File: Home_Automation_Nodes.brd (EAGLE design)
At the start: 121 x 70 mm, 19 parts

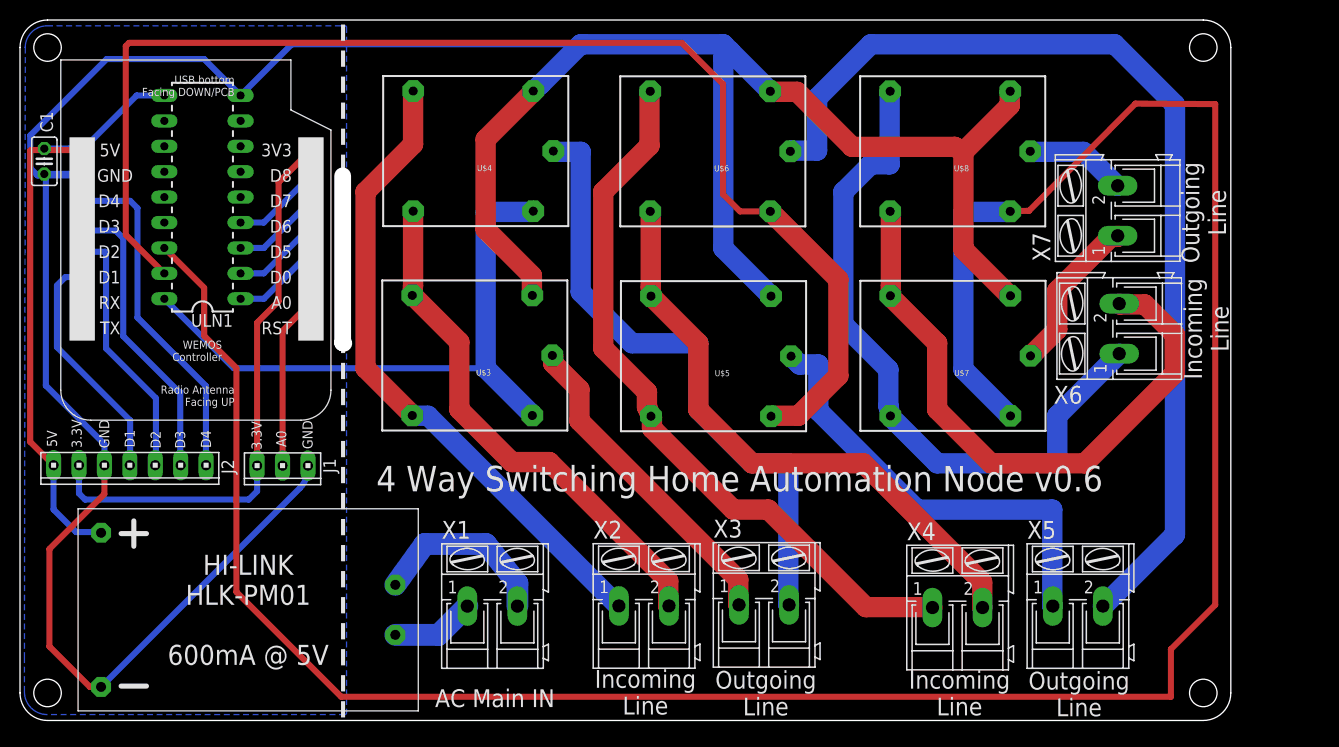
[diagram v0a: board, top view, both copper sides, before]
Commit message: ULN connection fix. Changed coil connection from GND to 5V
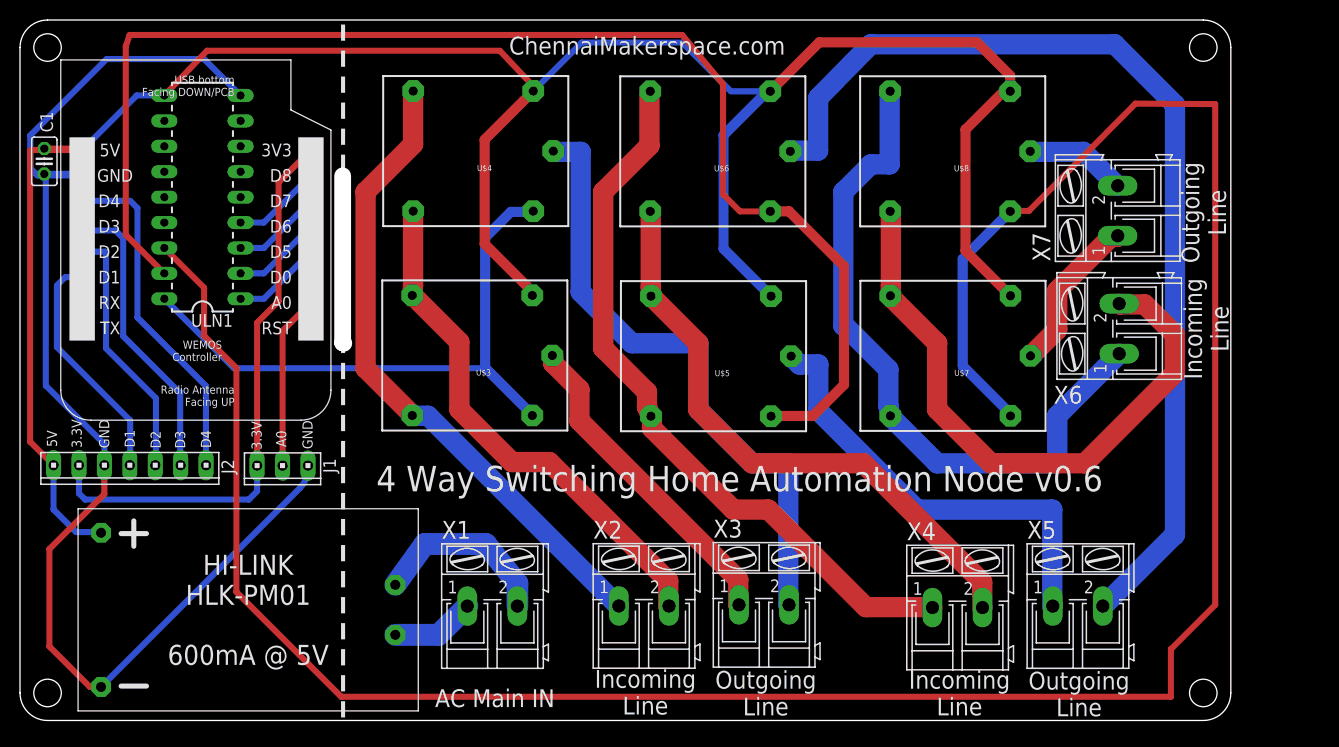
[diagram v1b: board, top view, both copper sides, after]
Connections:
- net 5V: now also U$3.COIL0, U$4.COIL0, U$5.COIL0, U$6.COIL0, U$7.COIL0, U$8.COIL0
- net GND: no longer U$3.COIL0, U$4.COIL0, U$5.COIL0, U$6.COIL0, U$7.COIL0, U$8.COIL0
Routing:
- net 5V: track 62.1 -> 233.0 mm, vias 0 -> 1
- net GND: track 288.8 -> 127.7 mm
- net RELAY2: track 129.9 -> 133.6 mm
- net RELAY3: track 248.2 -> 245.6 mm
- net RELAY1: track 62.1 -> 60.6 mm
- removed copper zone on layer 16, net GND
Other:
- board text added: "ChennaiMakerspace.com"

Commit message: Changes: 1. WeMos D1 Mini Pads modified 2. Pins to ULN changed, to free the SPI channels 3. GND Plane added
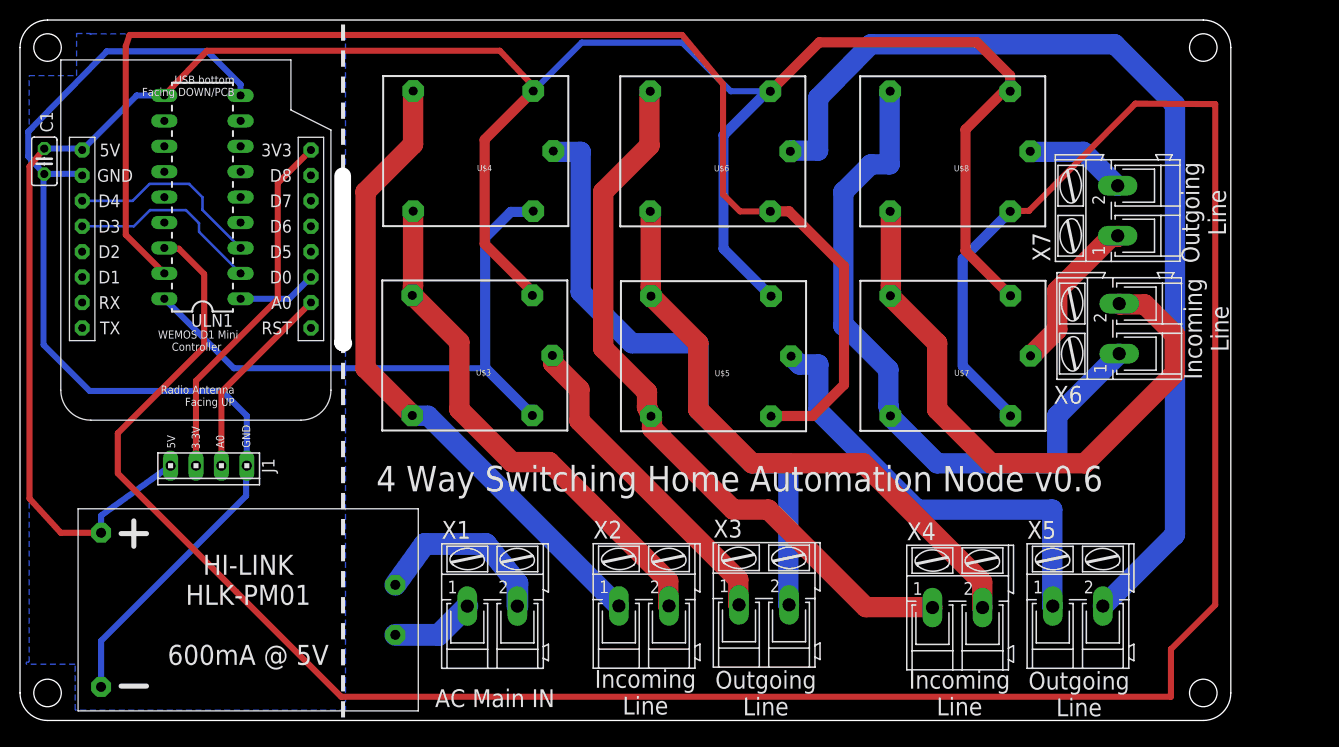
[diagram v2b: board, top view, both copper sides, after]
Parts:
- removed J2: (no value), con-amp:10X07MTA
- J1: device con-amp:10X03MTA -> con-amp:10X04MTA
- ULN1: value (none) -> ULN2803
- moved J1 7.38 mm to (18.9, 25.5)
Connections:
- removed net D3: J2.6, U$1.D3
- removed net D4: J2.7, U$1.D4
- removed net RELAY4: ULN1.15
- removed net SW4: U$1.D8, ULN1.4
- new net D5: U$1.D5
- new net D6: U$1.D6
- new net D7: U$1.D7
- net 3.3V: now also J1.2; no longer J1.1, J2.2
- net 5V: now also J1.1; no longer J2.1
- net A0: now also J1.3; no longer J1.2
- net D1: no longer J2.4
- net D2: no longer J2.5
- net GND: now also J1.4; no longer J1.3, J2.3
- net SW1: now also U$1.D0; no longer U$1.D5
- net SW2: now also U$1.D3; no longer U$1.D6
- net SW3: now also U$1.D4; no longer U$1.D7
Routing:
- net D4: track 34.4 -> 0.00 mm
- net D3: track 29.7 -> 0.00 mm
- net D2: track 25.8 -> 0.00 mm
- net D1: track 23.9 -> 0.00 mm
- net 3.3V: track 57.5 -> 36.3 mm
- net GND: track 127.7 -> 109.3 mm
- net SW3: track 8.98 -> 19.9 mm
- net SW2: track 8.98 -> 19.6 mm
- net SW4: track 8.98 -> 0.00 mm
- net RELAY3: track 245.6 -> 253.6 mm
- net 5V: track 233.0 -> 239.7 mm, vias 1 -> 0
- net A0: track 17.5 -> 20.0 mm
- net SW1: track 8.98 -> 7.93 mm
- added copper zone on layer 16, net GND
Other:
- board text added: "< --------- CAUTION: HIGH VOLTAGE --------- >"
- board text added: "Docs: github.com/Vijayenthiran"
- board text removed: "D1"
- board text removed: "D2"
- board text removed: "D3"
- board text removed: "D4"
